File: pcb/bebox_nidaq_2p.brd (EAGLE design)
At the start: 76.2 x 18.1 mm, 6 parts, among them J1 1-1634612-0, J2 1-1634612-0, J6 SJ-435107RS, U1 MCP23008-E/P, U2 MCP23008-E/P, X1 71430-0101

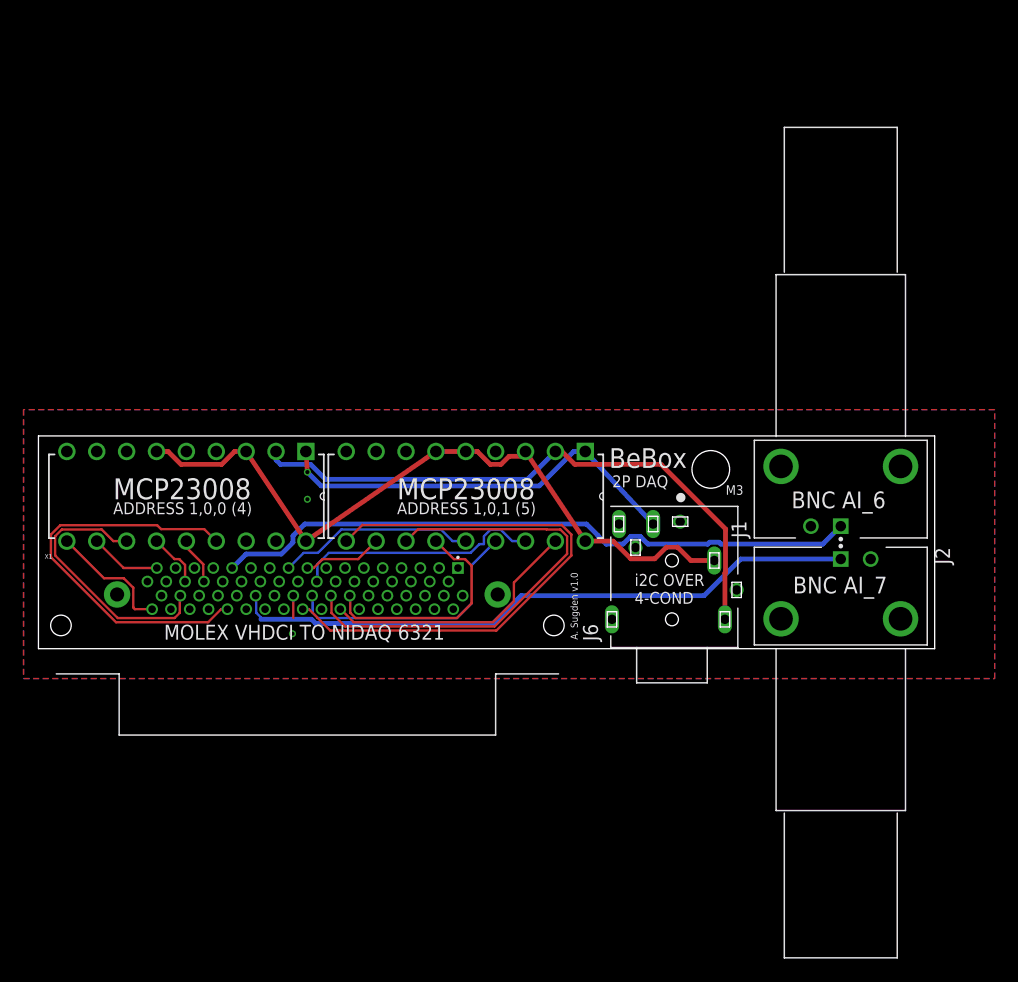
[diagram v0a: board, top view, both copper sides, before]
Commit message: Previously did not have sufficient analog inputs for two photometry inputs and one digital input. Now have 4 BNC inputs.
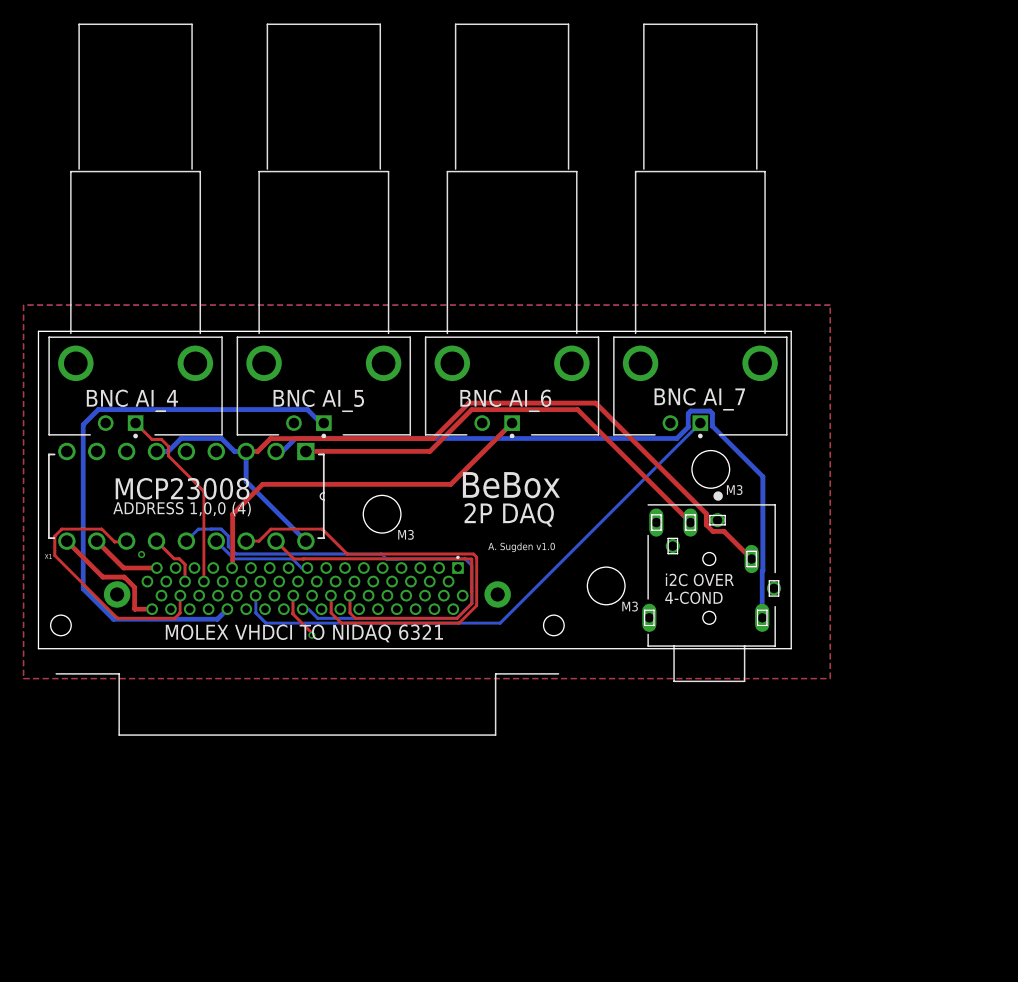
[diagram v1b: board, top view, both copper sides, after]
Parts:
- removed U1: MCP23008-E/P, MCP23008-E_P:DIP254P762X533-18
- added J3, J4: 1-1634612-0, 1-1634612-0:TE_1-1634612-0
- moved J1 29.3 mm to (40.3, 19.2)
- moved J2 16.6 mm to (56.3, 19.2), turned to 90 degrees
- moved J6 3.18 mm to (57.0, 6.22)
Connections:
- net 5V: no longer U1.18, U1.3, U1.5, U1.6
- net AI_4: now also J3.1; no longer U2.14
- net AI_5: now also J4.1; no longer U2.15
- net GND: now also J3.2, J4.2; no longer U1.4, U1.9
- net P0.0: now also U2.14; no longer U1.10
- net P0.1: now also U2.15; no longer U1.11
- net P0.2: now also U2.16; no longer U1.12
- net P0.3: now also U2.17; no longer U1.13
- net P0.4: no longer U1.14
- net P0.5: no longer U1.15
- net P0.6: no longer U1.16
- net P0.7: no longer U1.17
- net SCL: no longer U1.1
- net SDA: no longer U1.2
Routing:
- net AI_6: track 55.7 -> 31.6 mm
- net P0.7: track 22.5 -> 0.00 mm
- net P0.5: track 21.8 -> 0.00 mm
- net P0.6: track 21.2 -> 0.00 mm
- net P0.4: track 16.8 -> 0.00 mm
- net AI_5: track 34.6 -> 49.1 mm
- net P0.3: track 19.6 -> 33.6 mm
- net AI_4: track 4.05 -> 16.3 mm
- net 5V: track 61.4 -> 69.0 mm
- net SDA: track 51.0 -> 58.4 mm
- net AI_7: track 53.9 -> 46.7 mm
- net P0.0: track 48.1 -> 45.0 mm
- net SCL: track 35.5 -> 38.1 mm, vias 1 -> 0
- net GND: track 1.90 -> 4.08 mm
- net P0.1: track 6.79 -> 8.69 mm
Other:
- board size 76.2 x 18.1 mm -> 64 x 27 mm
- board text added: "BNC AI_4"
- board text added: "BNC AI_5"
- board text removed: "ADDRESS 1,0,1 (5)"
